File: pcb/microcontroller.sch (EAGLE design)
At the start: 8 parts

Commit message: microcontroller board ready to be fab'd
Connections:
- removed net N$2: X1.GPIO12
- net A0: now also X1.ADC
- net D6/GPIO12: now also X1.GPIO12
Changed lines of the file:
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@@
 <attribute name="VALUE" x="122.936" y="44.069" size="1.778" layer="96"/>
 </instance>
-<instance part="GND11" gate="1" x="121.92" y="38.1" smashed="yes">
-<attribute name="VALUE" x="119.38" y="35.56" size="1.778" layer="96"/>
+<instance part="GND11" gate="1" x="121.92" y="40.64" smashed="yes">
+<attribute name="VALUE" x="119.38" y="38.1" size="1.778" layer="96"/>
 </instance>
 <instance part="+3V4" gate="G$1" x="180.34" y="76.2" smashed="yes" rot="MR0">
@@
 <pinref part="C10" gate="G$1" pin="2"/>
 <pinref part="GND11" gate="1" pin="GND"/>
-<wire x1="121.92" y1="43.18" x2="121.92" y2="40.64" width="0.1524" layer="91"/>
 </segment>
 <segment>
@@
 <pinref part="X1" gate="G$1" pin="VCC"/>
 <pinref part="C10" gate="G$1" pin="1"/>
-<wire x1="121.92" y1="45.72" x2="121.92" y2="50.8" width="0.1524" layer="91"/>
-<wire x1="121.92" y1="45.72" x2="121.92" y2="53.34" width="0.1524" layer="91"/>
+<wire x1="121.92" y1="50.8" x2="121.92" y2="53.34" width="0.1524" layer="91"/>
 </segment>
 <segment>
@@
 <wire x1="124.46" y1="66.04" x2="116.84" y2="66.04" width="0.1524" layer="91"/>
 <pinref part="X1" gate="G$1" pin="CH_PD"/>
-<label x="116.84" y="66.04" size="1.778" layer="95"/>
+<label x="121.92" y="66.04" size="1.778" layer="95" rot="R180"/>
 </segment>
 </net>
@@
 <label x="160.02" y="5.08" size="1.778" layer="95"/>
 </segment>
+<segment>
+<pinref part="X1" gate="G$1" pin="GPIO12"/>
+<wire x1="124.46" y1="58.42" x2="121.92" y2="58.42" width="0.1524" layer="91"/>
+<label x="121.92" y="58.42" size="1.778" layer="95" rot="R180"/>
+</segment>
 </net>
 <net name="D5/GPIO14/SCK" class="0">
@@
 <label x="160.02" y="12.7" size="1.778" layer="95"/>
 </segment>
+<segment>
+<pinref part="X1" gate="G$1" pin="ADC"/>
+<wire x1="124.46" y1="68.58" x2="121.92" y2="68.58" width="0.1524" layer="91"/>
+<label x="121.92" y="68.58" size="1.778" layer="95" rot="R180"/>
+</segment>
 </net>
 <net name="D7/GPIO13/MOSI" class="0">
@@
 </segment>
 </net>
-<net name="N$2" class="0">
-<segment>
-<pinref part="X1" gate="G$1" pin="GPIO12"/>
-<wire x1="124.46" y1="58.42" x2="121.92" y2="58.42" width="0.1524" layer="91"/>
-</segment>
-</net>
 </nets>
 </sheet>
 </sheets>
-<errors>
-</errors>
 </schematic>
 </drawing>

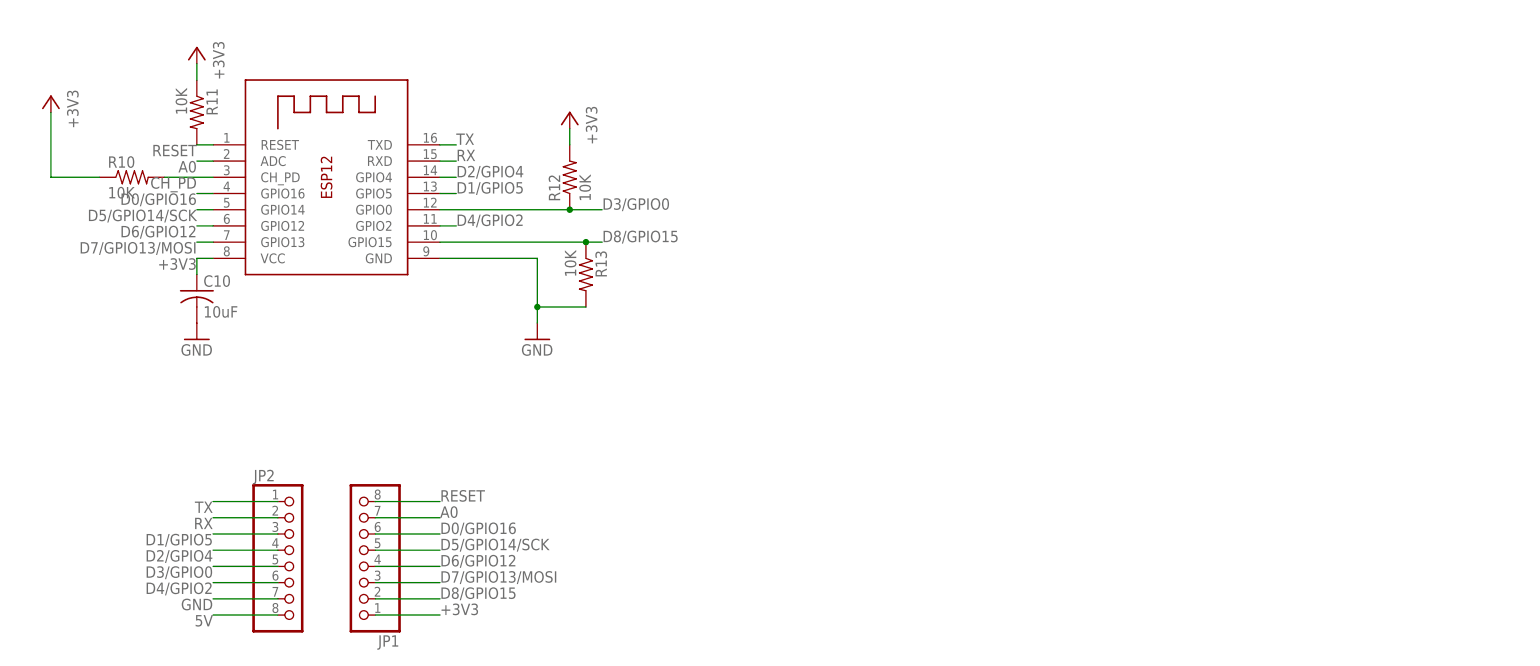
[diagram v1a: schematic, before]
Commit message: Microcontroller v2 pcb ordered
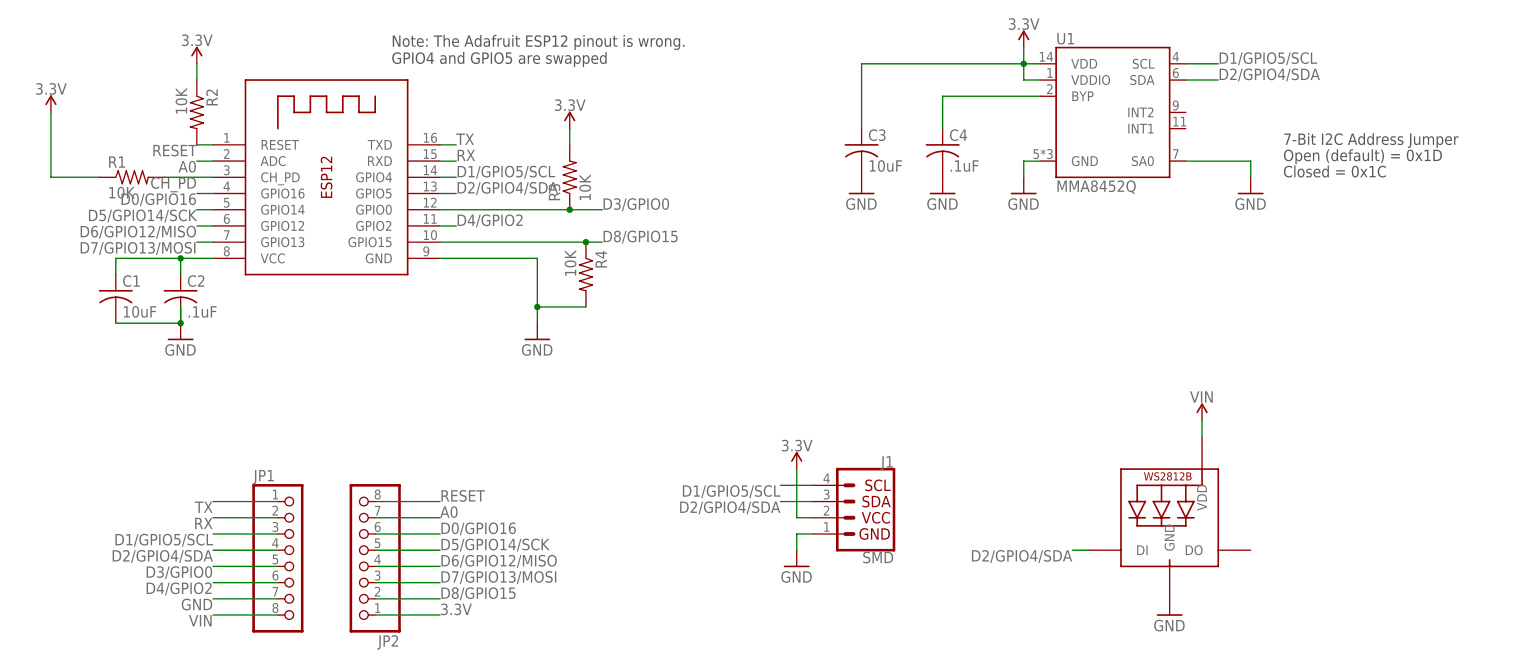
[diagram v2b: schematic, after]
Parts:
- removed C10: 10uF, adafruit:C-USC0805
- added C1, C3: 10uF, adafruit:C-USC0805
- added C2, C4: .1uF, adafruit:C-USC0805
- added J1: SMD, SparkX:I2C_STANDARDJS-1MM
- added LED1: WS2812B5050, adafruit:WS2812B5050
- added U1: MMA8452Q, SparkX:MMA8452Q
- JP1, JP2: MPN (none) -> 8Fx1L-254mm
- R1, R2, R3, R4: MPN (none) -> CRCW080510K0FKEAC
- X1: MPN (none) -> ESP12
- renumbered R10 to R1, R11 to R2, R12 to R3, R13 to R4
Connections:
- removed net +3V3: C10.1, JP1.1, R1.1, R2.1, R3.2, X1.VCC
- removed net 5V: JP2.8
- removed net D1/GPIO5: JP2.3, X1.GPIO5
- removed net D2/GPIO4: JP2.4, X1.GPIO4
- removed net D6/GPIO12: JP1.4, X1.GPIO12
- new net 3.3V: C3.1, J1.VCC, JP2.1, R1.1, R2.1, R3.2, U1.VDD, U1.VDDIO
- new net BYP: C4.1, U1.BYP
- new net D1/GPIO5/SCL: J1.SCL, JP1.3, U1.SCL, X1.GPIO4
- new net D2/GPIO4/SDA: J1.SDA, JP1.4, LED1.DI, U1.SDA, X1.GPIO5
- new net D6/GPIO12/MISO: JP2.4, X1.GPIO12
- new net N$1: C1.1, C2.1, X1.VCC
- new net VIN: JP1.8, LED1.VDD
- net A0: now also JP2.7; no longer JP1.7
- net D0/GPIO16: now also JP2.6; no longer JP1.6
- net D3/GPIO0: now also JP1.5; no longer JP2.5
- net D4/GPIO2: now also JP1.6; no longer JP2.6
- net D5/GPIO14/SCK: now also JP2.5; no longer JP1.5
- net D7/GPIO13/MOSI: now also JP2.3; no longer JP1.3
- net D8/GPIO15: now also JP2.2; no longer JP1.2
- net GND: now also C1.2, C2.2, C3.2, C4.2, J1.GND, JP1.7, LED1.GND, U1.GND, U1.SA0; no longer C10.2, JP2.7
- net RESET: now also JP2.8; no longer JP1.8
- net RX: now also JP1.2; no longer JP2.2
- net TX: now also JP1.1; no longer JP2.1
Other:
- note added: "7-Bit I2C Address Jumper"
- note added: "Closed = 0x1C"
- note added: "Note: The Adafruit ESP12 pinout is wrong. GPIO4 and GPIO5 are swapped"
- note added: "Open (default) = 0x1D"
- moved on the sheet: JP1, JP2

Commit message: Use cheaper 0.1uF capacitors and 10uF capacitors
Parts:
- C1, C3: MPN EMK212ABJ106KG-T -> LMK212BJ106KG-T
- C2, C4: MPN 08051C104J4T4A -> C0805C104M3RACTU
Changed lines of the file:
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@@
 <parts>
 <part name="C1" library="adafruit" library_urn="urn:adsk.eagle:library:420" deviceset="C-US" device="C0805" package3d_urn="urn:adsk.eagle:package:6240337/1" value="10uF">
-<attribute name="MPN" value="EMK212ABJ106KG-T"/>
+<attribute name="MPN" value="LMK212BJ106KG-T"/>
 </part>
 <part name="GND1" library="supply1" deviceset="GND" device=""/>
@@
 <part name="SUPPLY4" library="SparkFun-PowerSymbols" library_urn="urn:adsk.eagle:library:530" deviceset="VIN" device=""/>
 <part name="C2" library="adafruit" library_urn="urn:adsk.eagle:library:420" deviceset="C-US" device="C0805" package3d_urn="urn:adsk.eagle:package:6240337/1" value=".1uF">
-<attribute name="MPN" value="08051C104J4T4A"/>
+<attribute name="MPN" value="C0805C104M3RACTU"/>
 </part>
 <part name="C4" library="adafruit" library_urn="urn:adsk.eagle:library:420" deviceset="C-US" device="C0805" package3d_urn="urn:adsk.eagle:package:6240337/1" value=".1uF">
-<attribute name="MPN" value="08051C104J4T4A"/>
+<attribute name="MPN" value="C0805C104M3RACTU"/>
 <attribute name="POPULATE" value="0"/>
 </part>
 <part name="C3" library="adafruit" library_urn="urn:adsk.eagle:library:420" deviceset="C-US" device="C0805" package3d_urn="urn:adsk.eagle:package:6240337/1" value="10uF">
-<attribute name="MPN" value="EMK212ABJ106KG-T"/>
+<attribute name="MPN" value="LMK212BJ106KG-T"/>
 <attribute name="POPULATE" value="0"/>
 </part>

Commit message: Fix microcontroller board to actually connect 3.3V to the microcontroller
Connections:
- removed net N$1: C1.1, C2.1, X1.VCC
- net 3.3V: now also C1.1, C2.1, X1.VCC
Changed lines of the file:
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@@
 <?xml version="1.0" encoding="utf-8"?>
 <!DOCTYPE eagle SYSTEM "eagle.dtd">
-<eagle version="9.5.1">
+<eagle version="9.6.2">
 <drawing>
 <settings>
@@
 <part name="SUPPLY5" library="SparkFun-PowerSymbols" deviceset="3.3V" device=""/>
 <part name="SUPPLY6" library="SparkFun-PowerSymbols" deviceset="3.3V" device=""/>
+<part name="SUPPLY7" library="SparkFun-PowerSymbols" deviceset="3.3V" device=""/>
 </parts>
 <sheets>
@@
 <attribute name="VALUE" x="99.06" y="78.994" size="1.778" layer="96" align="bottom-center"/>
 </instance>
+<instance part="SUPPLY7" gate="G$1" x="96.52" y="53.34" smashed="yes">
+<attribute name="VALUE" x="96.52" y="56.134" size="1.778" layer="96" align="bottom-center"/>
+</instance>
 </instances>
 <busses>
@@
 <pinref part="SUPPLY5" gate="G$1" pin="3.3V"/>
 </segment>
-</net>
-<net name="N$1" class="1">
 <segment>
 <pinref part="C1" gate="G$1" pin="1"/>
@@
 <wire x1="119.38" y1="53.34" x2="119.38" y2="50.8" width="0.1524" layer="91"/>
 <junction x="119.38" y="53.34"/>
-</segment>
-</net>
+<pinref part="SUPPLY7" gate="G$1" pin="3.3V"/>
+<wire x1="109.22" y1="53.34" x2="96.52" y2="53.34" width="0.1524" layer="91"/>
+<junction x="109.22" y="53.34"/>
+</segment>
+</net>
